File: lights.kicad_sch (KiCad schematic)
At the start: 27 parts, among them Q1 2N7002, Q2 2N7002, U1 EL3H7

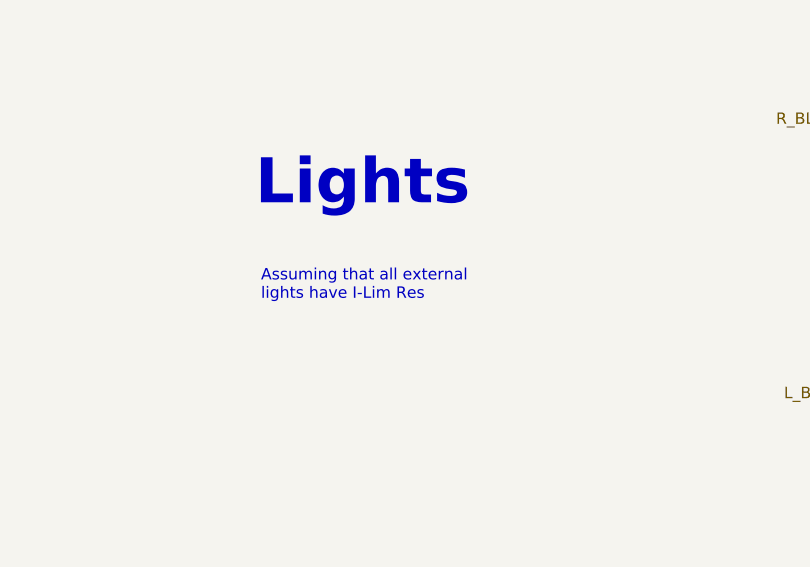
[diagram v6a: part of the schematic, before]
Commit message: Adjusted & added footprints, several minor changes
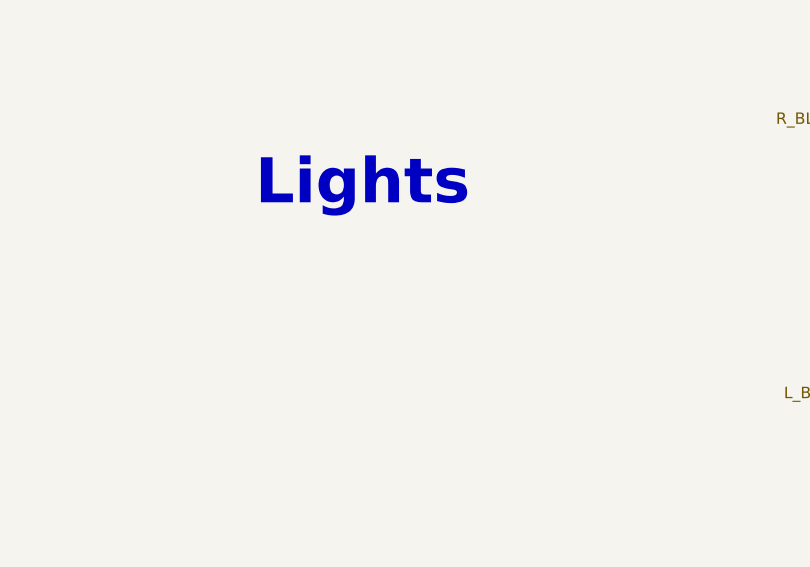
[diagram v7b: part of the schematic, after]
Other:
- note removed: "Assuming that all external lights have I-Lim Res"
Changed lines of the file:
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@@
     (stroke (width 0) (type default))
-  )
-  (text "Assuming that all external \nlights have I-Lim Res" (at 106.045 46.355 0)
-    (effects (font (size 1.27 1.27)) (justify left bottom))
   )
   (text "Lights" (at 105.41 36.195 0)

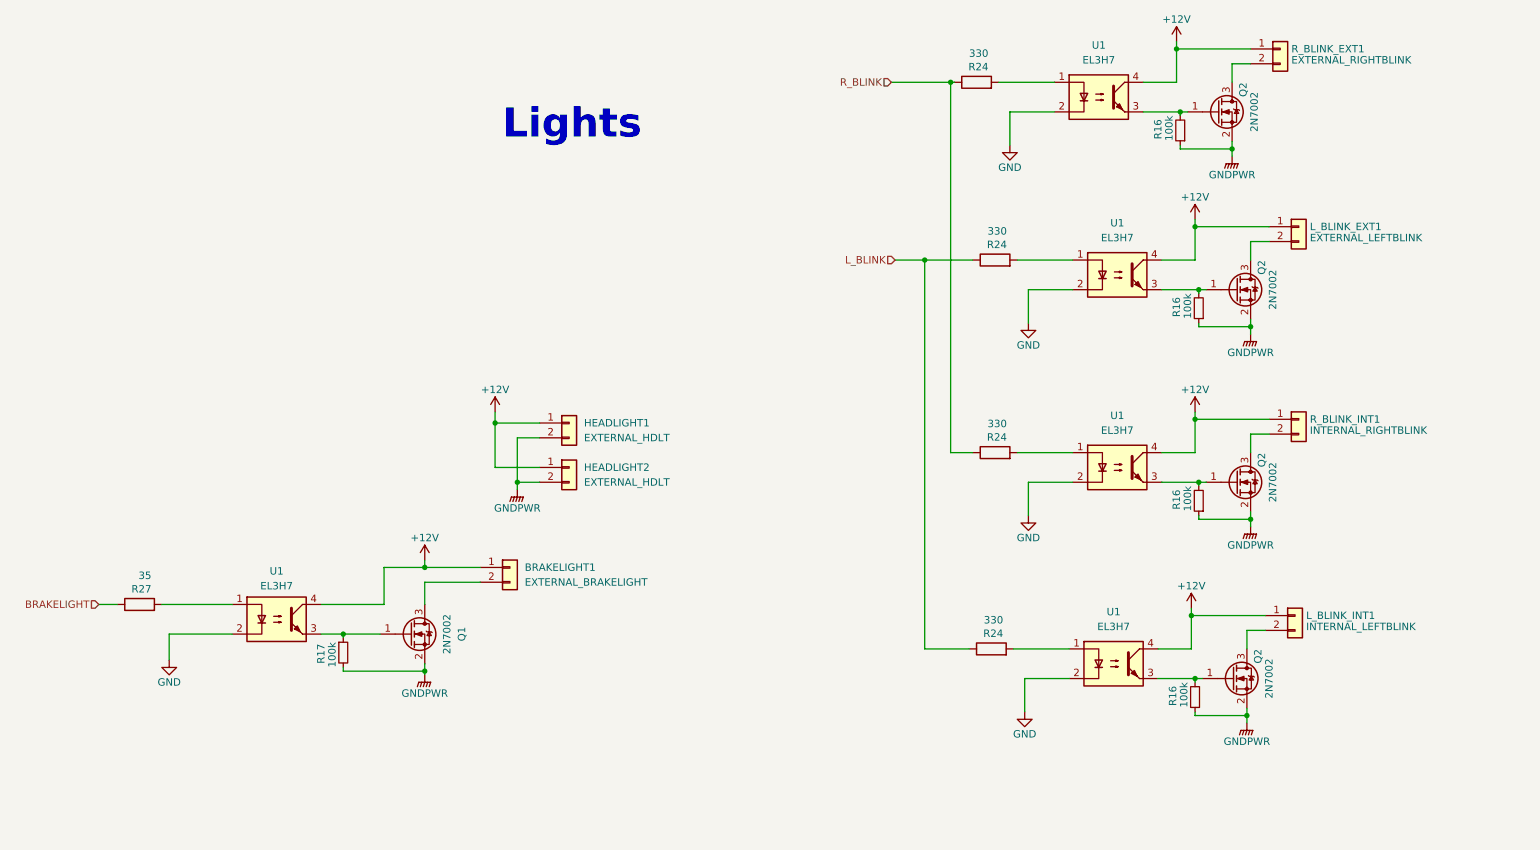
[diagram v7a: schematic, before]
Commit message: Changed optocoupler resistor values, updated Mouser PNs
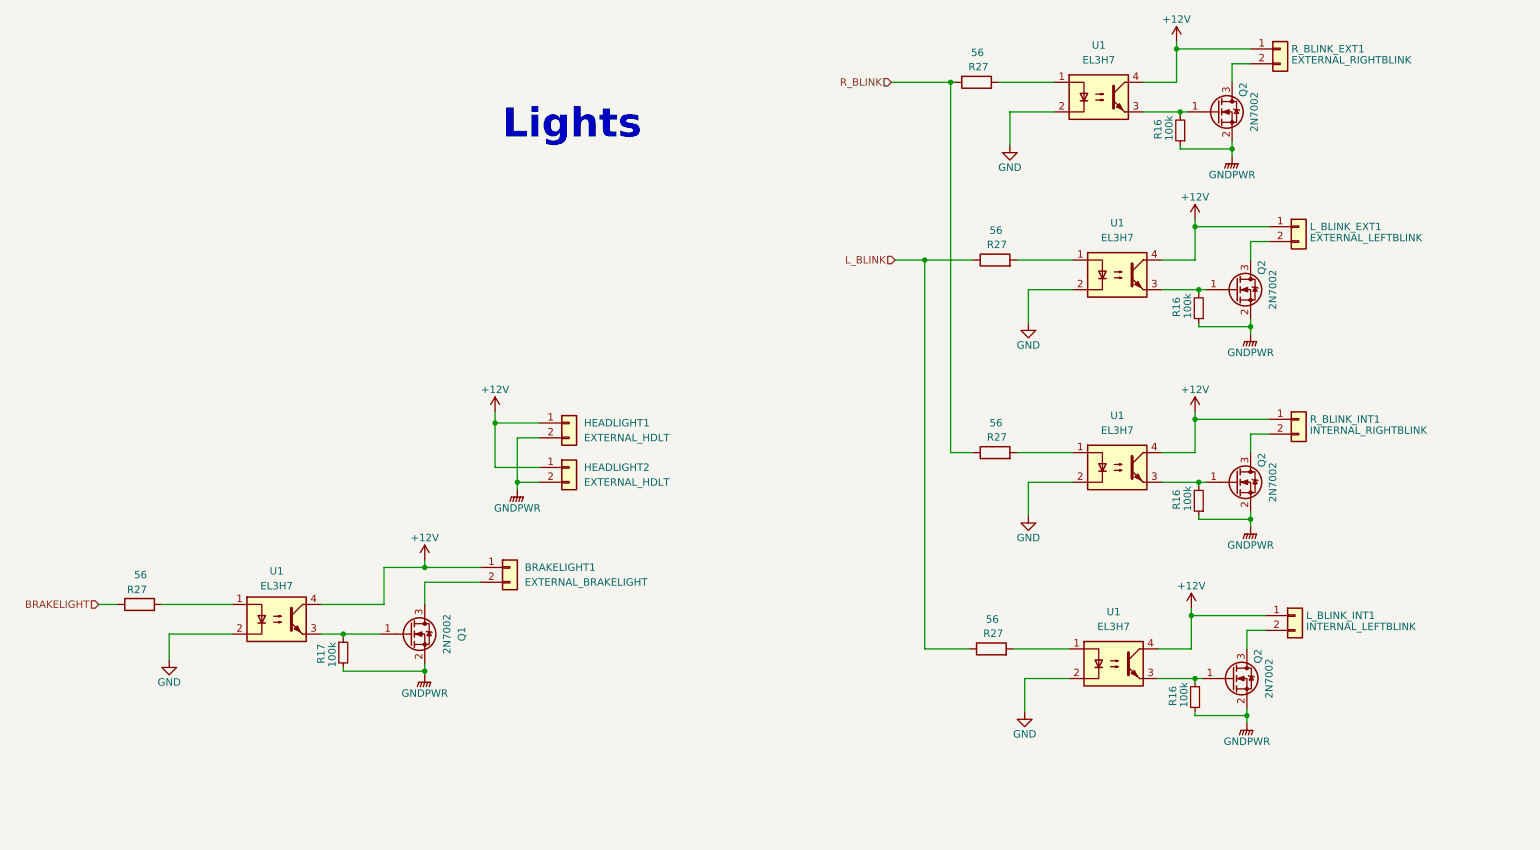
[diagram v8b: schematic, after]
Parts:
- removed R24 (x4): 330, Resistor_SMD:R_0805_2012Metric, symbol Device:R
- removed R27: 35, Resistor_SMD:R_0805_2012Metric, symbol Device:R
- added R27 (x5): 56, Resistor_SMD:R_0805_2012Metric, symbol Device:R
- BRAKELIGHT1, R_BLINK_EXT1, R_BLINK_INT1: Mauser PN 538-43650-0215 -> (none); Mouser PN (none) -> 538-43650-0215
- HEADLIGHT1, HEADLIGHT2, L_BLINK_EXT1, L_BLINK_INT1: Mouser PN (none) -> 538-43650-0215
- Q1, Q2: Mauser PN 771-2N7002HR -> (none); Mouser PN (none) -> 771-2N7002HR
- R16, R17: Mauser PN 71-CRCW0805100KFKEAC -> (none); Mouser PN (none) -> 71-CRCW0805100KFKEAC
- U1: Mauser PN 638-EL3H7DTAVG -> (none); Mouser PN (none) -> 638-EL3H7DTAVG
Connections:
- net BRAKELIGHT: now also R27.1
- net L_BLINK: now also R27.1, R27.1
- net R_BLINK: now also R27.1, R27.1
- net at U1.1: now also R27.2 (x5)
